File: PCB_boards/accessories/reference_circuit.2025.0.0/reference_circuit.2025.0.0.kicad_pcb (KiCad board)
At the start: 2 copper layers, 75 x 50 mm, 41 parts, among them J1 Conn_02x08_Odd_Even, J2 Screw_Terminal_01x04

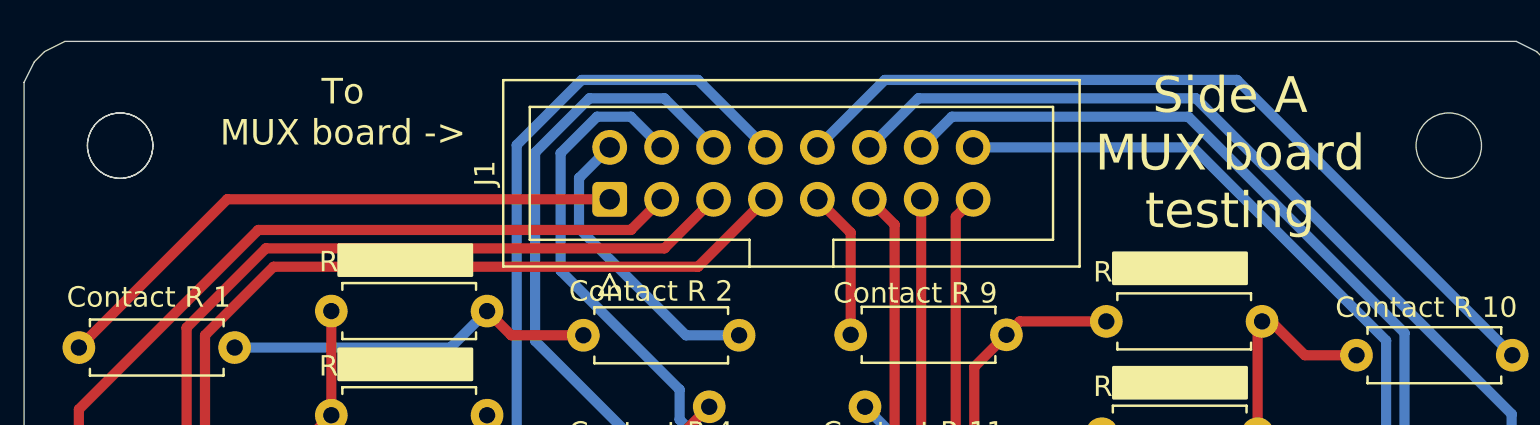
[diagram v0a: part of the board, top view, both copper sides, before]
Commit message: adds new reference circuit #260
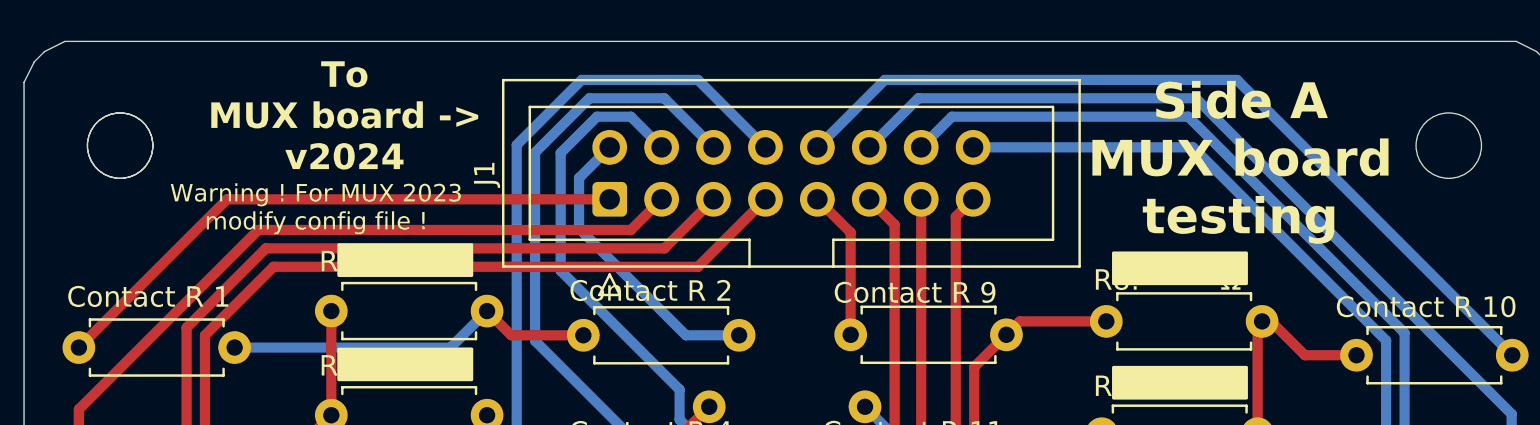
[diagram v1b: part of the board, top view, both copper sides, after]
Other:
- board text added: "To MUX board -> v2024"
- board text added: "Warning ! For MUX 2023 modify config file !"
- board text removed: "To MUX board ->"
